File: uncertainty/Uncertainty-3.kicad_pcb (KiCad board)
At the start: 2 copper layers, 58.8 x 128.5 mm, 70 parts, among them J1 SWITCHCRAFT_35RASMT2AHNTRX, J10 SAMTEC_TSM-103-01-L-SH, J2 SWITCHCRAFT_35RASMT2AHNTRX, J3 SWITCHCRAFT_35RASMT2AHNTRX, J4 SWITCHCRAFT_35RASMT2AHNTRX, J5 SWITCHCRAFT_35RASMT2AHNTRX, J6 SWITCHCRAFT_35RASMT2AHNTRX, J7 SWITCHCRAFT_35RASMT2AHNTRX, J8 SWITCHCRAFT_35RASMT2AHNTRX, J9 SWITCHCRAFT_35RASMT2AHNTRX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

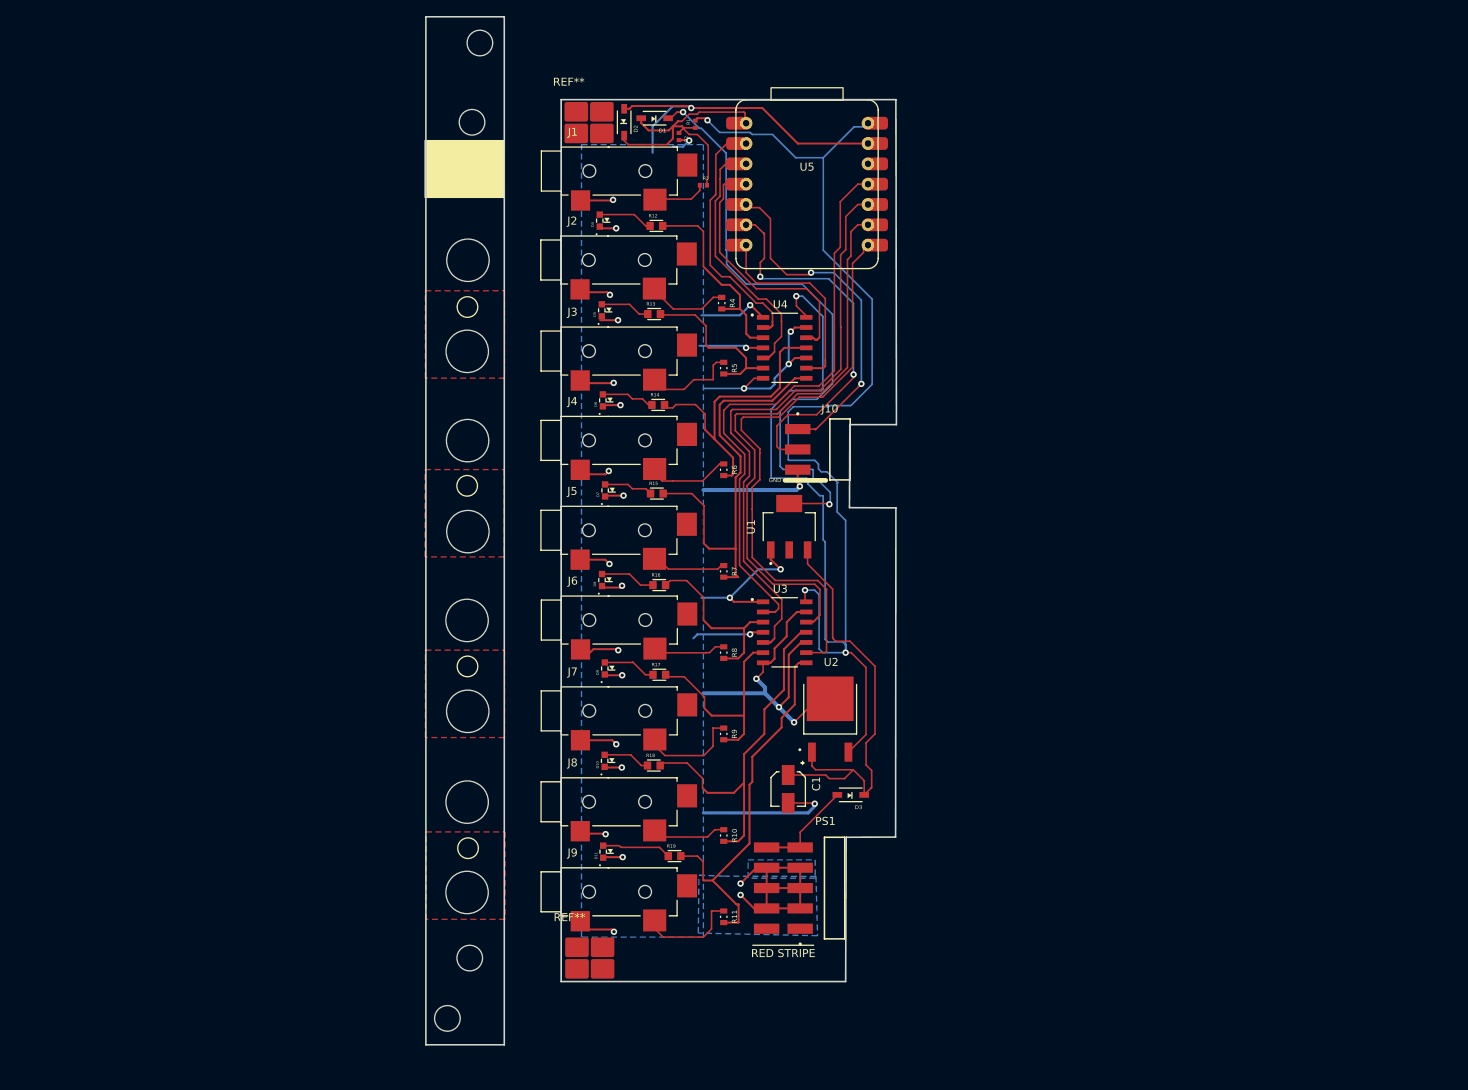
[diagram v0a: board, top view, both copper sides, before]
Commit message: New LEDs added
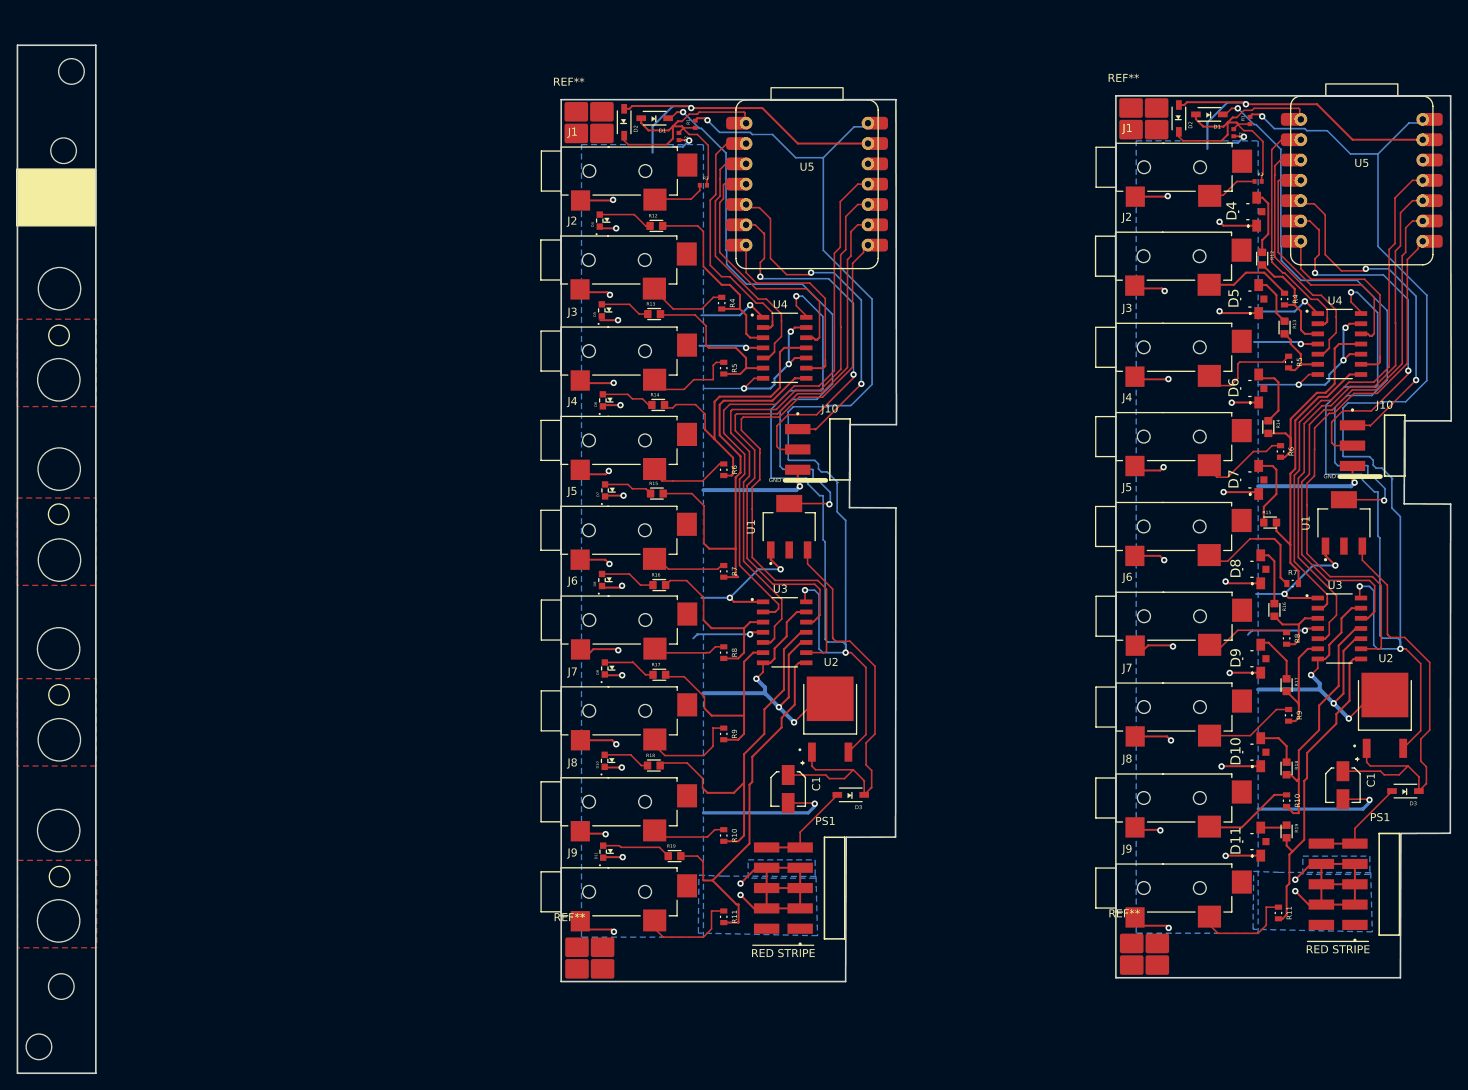
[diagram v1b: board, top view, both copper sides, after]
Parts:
- added C1: CAP_EEE-FT1E220AR, Import Library:CAP_EEE-FT1E220AR, F.Cu at (208.7, 115.6)
- added D1: SOD3715X145N, Import Library:Diode-1N5819HW-7-F, F.Cu at (192.0, 31.8)
- added D10: APPA3010SURCK, Import Library:LED-SMD Red SideEmit Angle30 3x1mm -APPA3010SURCK, F.Cu at (197.9, 111.5)
- added D11: APPA3010SURCK, Import Library:LED-SMD Red SideEmit Angle30 3x1mm -APPA3010SURCK, F.Cu at (197.9, 122.7)
- added D2: SOD3715X145N, Import Library:Diode-1N5819HW-7-F, F.Cu at (188.2, 32.3)
- added D3: SOD3715X145N, Import Library:Diode-1N5819HW-7-F, F.Cu at (216.5, 116.4)
- added D4: APPA3010SURCK, Import Library:LED-SMD Red SideEmit Angle30 3x1mm -APPA3010SURCK, F.Cu at (197.4, 43.9)
- added D5: APPA3010SURCK, Import Library:LED-SMD Red SideEmit Angle30 3x1mm -APPA3010SURCK, F.Cu at (197.6, 54.9)
- added D6: APPA3010SURCK, Import Library:LED-SMD Red SideEmit Angle30 3x1mm -APPA3010SURCK, F.Cu at (197.6, 66.0)
- added D7: APPA3010SURCK, Import Library:LED-SMD Red SideEmit Angle30 3x1mm -APPA3010SURCK, F.Cu at (197.6, 77.5)
- added D8: APPA3010SURCK, Import Library:LED-SMD Red SideEmit Angle30 3x1mm -APPA3010SURCK, F.Cu at (197.9, 88.6)
- added D9: APPA3010SURCK, Import Library:LED-SMD Red SideEmit Angle30 3x1mm -APPA3010SURCK, F.Cu at (197.9, 99.8)
- added J1: SWITCHCRAFT_35RASMT2AHNTRX, Import Library:SWITCHCRAFT_35RASMT2AHNTRX, F.Cu at (180.4, 38.4)
- added J10: SAMTEC_TSM-103-01-L-SH, Import Library:SAMTEC_TSM-103-01-L-SH, F.Cu at (215.2, 73.2)
- added J2: SWITCHCRAFT_35RASMT2AHNTRX, Import Library:SWITCHCRAFT_35RASMT2AHNTRX, F.Cu at (180.3, 49.5)
- added J3: SWITCHCRAFT_35RASMT2AHNTRX, Import Library:SWITCHCRAFT_35RASMT2AHNTRX, F.Cu at (180.3, 60.9)
- added J4: SWITCHCRAFT_35RASMT2AHNTRX, Import Library:SWITCHCRAFT_35RASMT2AHNTRX, F.Cu at (180.3, 72.1)
- added J5: SWITCHCRAFT_35RASMT2AHNTRX, Import Library:SWITCHCRAFT_35RASMT2AHNTRX, F.Cu at (180.3, 83.3)
- added J6: SWITCHCRAFT_35RASMT2AHNTRX, Import Library:SWITCHCRAFT_35RASMT2AHNTRX, F.Cu at (180.4, 94.5)
- added J7: SWITCHCRAFT_35RASMT2AHNTRX, Import Library:SWITCHCRAFT_35RASMT2AHNTRX, F.Cu at (180.3, 105.9)
- added J8: SWITCHCRAFT_35RASMT2AHNTRX, Import Library:SWITCHCRAFT_35RASMT2AHNTRX, F.Cu at (180.3, 117.2)
- added J9: SWITCHCRAFT_35RASMT2AHNTRX, Import Library:SWITCHCRAFT_35RASMT2AHNTRX, F.Cu at (180.3, 128.5)
- added PS1: SAMTEC_TSM-105-01-L-DH, Import Library:SAMTEC_TSM-105-01-L-DH, F.Cu at (214.5, 128.0)
- added R1: In Resist-ERJ-2RKF1003X, Import Library:In Resist-ERJ-2RKF1003X, F.Cu at (197.1, 32.5)
- added R10: Out Resist-RES_ERJPA3D1001V, Import Library:Out Resist-RES_ERJPA3D1001V, F.Cu at (201.7, 117.6)
- added R11: Out Resist-RES_ERJPA3D1001V, Import Library:Out Resist-RES_ERJPA3D1001V, F.Cu at (200.7, 131.6)
- added R12: RESC1608X50N, Import Library:RESC1608X50N, F.Cu at (198.6, 49.8)
- added R13: RESC1608X50N, Import Library:RESC1608X50N, F.Cu at (201.4, 58.4)
- added R14: RESC1608X50N, Import Library:RESC1608X50N, F.Cu at (199.4, 70.9)
- added R15: RESC1608X50N, Import Library:RESC1608X50N, F.Cu at (199.6, 82.8)
- added R16: RESC1608X50N, Import Library:RESC1608X50N, F.Cu at (200.2, 93.7)
- added R17: RESC1608X50N, Import Library:RESC1608X50N, F.Cu at (201.7, 103.1)
- added R18: RESC1608X50N, Import Library:RESC1608X50N, F.Cu at (201.7, 113.5)
- added R19: RESC1608X50N, Import Library:RESC1608X50N, F.Cu at (201.7, 121.4)
- added R2: In Resist-ERJ-2RKF1003X, Import Library:In Resist-ERJ-2RKF1003X, F.Cu at (195.1, 34.1)
- added R3: In Resist-ERJ-2RKF1003X, Import Library:In Resist-ERJ-2RKF1003X, F.Cu at (198.1, 40.2)
- added R4: Out Resist-RES_ERJPA3D1001V, Import Library:Out Resist-RES_ERJPA3D1001V, F.Cu at (201.4, 54.9)
- added R5: Out Resist-RES_ERJPA3D1001V, Import Library:Out Resist-RES_ERJPA3D1001V, F.Cu at (201.9, 62.7)
- added R6: Out Resist-RES_ERJPA3D1001V, Import Library:Out Resist-RES_ERJPA3D1001V, F.Cu at (200.9, 73.9)
- added R7: Out Resist-RES_ERJPA3D1001V, Import Library:Out Resist-RES_ERJPA3D1001V, F.Cu at (202.4, 90.4)
- added R8: Out Resist-RES_ERJPA3D1001V, Import Library:Out Resist-RES_ERJPA3D1001V, F.Cu at (201.7, 97.3)
- added R9: Out Resist-RES_ERJPA3D1001V, Import Library:Out Resist-RES_ERJPA3D1001V, F.Cu at (201.9, 106.9)
- added REF**: Wurth 7466303, Import Library:Hardware-Right angle SMT mounting block-Wurth 7466303, F.Cu at (183.9, 136.8)
- added REF**: Wurth 7466303, Import Library:Hardware-Right angle SMT mounting block-Wurth 7466303, F.Cu at (183.8, 32.3)
- added U1: VREG_LM1117IMPX-3.3/NOPB, Import Library:VREG_LM1117IMPX-3.3_NOPB, F.Cu at (208.8, 82.8)
- added U2: VREG_L7805CDT-TR, Import Library:VREG_L7805CDT-TR, F.Cu at (214.0, 106.8)
- added U3: SN74HCS125QDRQ1, Import Library:Quad Bus-SMD SN74HCS125QDRQ1, F.Cu at (208.3, 96.0)
- added U4: SN74HCS125QDRQ1, Import Library:Quad Bus-SMD SN74HCS125QDRQ1, F.Cu at (208.3, 60.5)
- added U5: XIAO-RP2040, Import Library:XIAO-RP2040, F.Cu at (202.2, 50.6)
- moved REF** 51.2 mm to (48.3, 87.5)
- moved REF** 51.2 mm to (48.2, 121.3)
- moved REF** 51.2 mm to (48.2, 132.6)
- moved REF** 51.2 mm to (48.2, 65.0)
- moved REF** 51.2 mm to (48.8, 36.3)
- moved REF** 51.2 mm to (48.2, 42.2)
- moved REF** 51.2 mm to (45.7, 148.3)
- moved REF** 51.2 mm to (48.3, 93.0)
- moved REF** 51.2 mm to (48.3, 110.0)
- moved REF** 51.2 mm to (48.3, 53.6)
- moved REF** 51.2 mm to (48.3, 48.0)
- moved REF** 51.2 mm to (49.8, 26.4)
- moved REF** 51.2 mm to (48.3, 59.4)
- moved REF** 51.2 mm to (48.3, 70.6)
- moved REF** 51.2 mm to (48.3, 115.8)
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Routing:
- net (no net): track 1535.8 -> 2979.1 mm, vias 42 -> 83
- net ground: track 45.5 -> 94.6 mm, vias 2 -> 5
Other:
- board size 58.8 x 128.5 mm -> 179.2 x 128.5 mm
